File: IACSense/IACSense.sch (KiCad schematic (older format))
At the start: 86 parts, among them P1 IN, P2 OUT, P3 zcd, P4 event, P5 Prog, P6 +3.3v, P7 I2C, P8 Test, SW1 SW_Push, U1 MCP39F521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

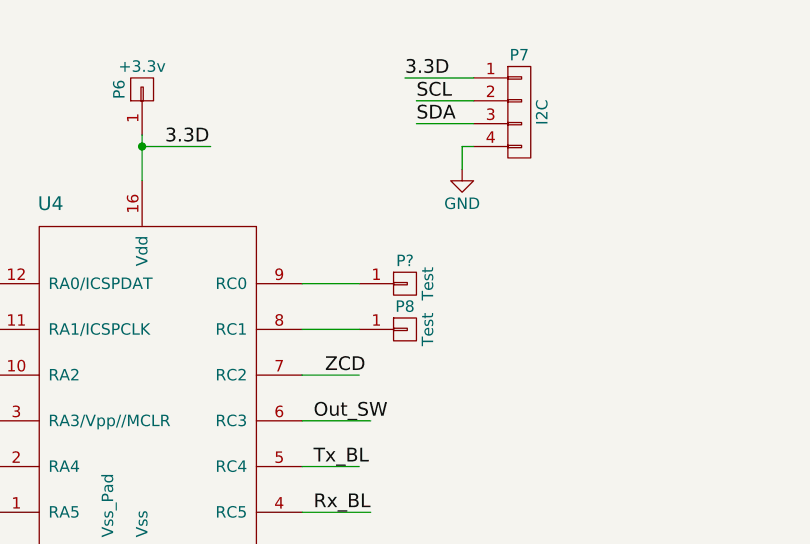
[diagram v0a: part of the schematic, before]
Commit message: place all components on DAC_Analog
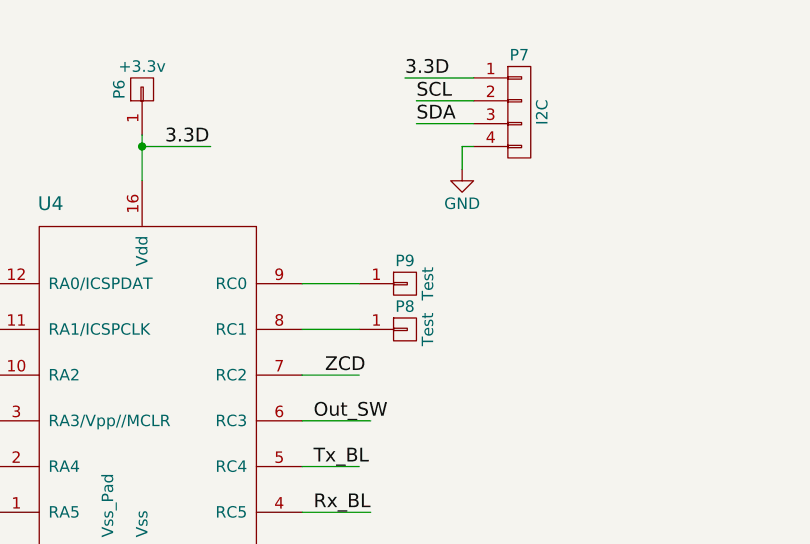
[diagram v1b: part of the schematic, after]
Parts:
- P7: footprint Pin_Headers:Pin_Header_Straight_1x04_Pitch1.00mm -> Pin_Headers:Pin_Header_Straight_1x04_Pitch1.27mm
- gave numbers to parts that had none: 1
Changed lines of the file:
@@
 $EndComp
 $Comp
-L GND #PWR2
+L GND #PWR01
 U 1 1 56D34A90
 P 3700 1950
-F 0 "#PWR2" H 3700 1700 50  0001 C CNN
+F 0 "#PWR01" H 3700 1700 50  0001 C CNN
 F 1 "GND" H 3700 1800 50  0000 C CNN
 F 2 "" H 3700 1950 60  0000 C CNN
@@
 $EndComp
 $Comp
-L GND #PWR4
+L GND #PWR02
 U 1 1 56D35186
 P 4750 2950
-F 0 "#PWR4" H 4750 2700 50  0001 C CNN
+F 0 "#PWR02" H 4750 2700 50  0001 C CNN
 F 1 "GND" H 4750 2800 50  0000 C CNN
 F 2 "" H 4750 2950 60  0000 C CNN
@@
 $EndComp
 $Comp
-L GND #PWR3
+L GND #PWR03
 U 1 1 56D35ED8
 P 4350 3900
-F 0 "#PWR3" H 4350 3650 50  0001 C CNN
+F 0 "#PWR03" H 4350 3650 50  0001 C CNN
 F 1 "GND" H 4350 3750 50  0000 C CNN
 F 2 "" H 4350 3900 60  0000 C CNN
@@
 $EndComp
 $Comp
-L GND #PWR5
+L GND #PWR04
 U 1 1 56D366F0
 P 4950 4750
-F 0 "#PWR5" H 4950 4500 50  0001 C CNN
+F 0 "#PWR04" H 4950 4500 50  0001 C CNN
 F 1 "GND" H 4950 4600 50  0000 C CNN
 F 2 "" H 4950 4750 60  0000 C CNN
@@
 $EndComp
 $Comp
-L GND #PWR8
+L GND #PWR05
 U 1 1 56D36767
 P 5250 4750
-F 0 "#PWR8" H 5250 4500 50  0001 C CNN
+F 0 "#PWR05" H 5250 4500 50  0001 C CNN
 F 1 "GND" H 5250 4600 50  0000 C CNN
 F 2 "" H 5250 4750 60  0000 C CNN
@@
 $EndComp
 $Comp
-L GND #PWR14
+L GND #PWR06
 U 1 1 56D37BE1
 P 7000 2750
-F 0 "#PWR14" H 7000 2500 50  0001 C CNN
+F 0 "#PWR06" H 7000 2500 50  0001 C CNN
 F 1 "GND" H 7000 2600 50  0000 C CNN
 F 2 "" H 7000 2750 60  0000 C CNN
@@
 $EndComp
 $Comp
-L GND #PWR10
+L GND #PWR07
 U 1 1 56D38721
 P 5900 4300
-F 0 "#PWR10" H 5900 4050 50  0001 C CNN
+F 0 "#PWR07" H 5900 4050 50  0001 C CNN
 F 1 "GND" H 5900 4150 50  0000 C CNN
 F 2 "" H 5900 4300 60  0000 C CNN
@@
 $EndComp
 $Comp
-L GND #PWR11
+L GND #PWR08
 U 1 1 56D3887C
 P 6000 4500
-F 0 "#PWR11" H 6000 4250 50  0001 C CNN
+F 0 "#PWR08" H 6000 4250 50  0001 C CNN
 F 1 "GND" H 6000 4350 50  0000 C CNN
 F 2 "" H 6000 4500 60  0000 C CNN
@@
 $EndComp
 $Comp
-L GND #PWR12
+L GND #PWR09
 U 1 1 56D38905
 P 6200 4300
-F 0 "#PWR12" H 6200 4050 50  0001 C CNN
+F 0 "#PWR09" H 6200 4050 50  0001 C CNN
 F 1 "GND" H 6200 4150 50  0000 C CNN
 F 2 "" H 6200 4300 60  0000 C CNN
@@
 $EndComp
 $Comp
-L GND #PWR13
+L GND #PWR010
 U 1 1 56D38BD8
 P 6850 4250
-F 0 "#PWR13" H 6850 4000 50  0001 C CNN
+F 0 "#PWR010" H 6850 4000 50  0001 C CNN
 F 1 "GND" H 6850 4100 50  0000 C CNN
 F 2 "" H 6850 4250 60  0000 C CNN
@@
 $EndComp
 $Comp
-L GND #PWR15
+L GND #PWR011
 U 1 1 56D38CDF
 P 7150 4250
-F 0 "#PWR15" H 7150 4000 50  0001 C CNN
+F 0 "#PWR011" H 7150 4000 50  0001 C CNN
 F 1 "GND" H 7150 4100 50  0000 C CNN
 F 2 "" H 7150 4250 60  0000 C CNN
@@
 $EndComp
 $Comp
-L GND #PWR17
+L GND #PWR012
 U 1 1 56D3A7BB
 P 7750 4350
-F 0 "#PWR17" H 7750 4100 50  0001 C CNN
+F 0 "#PWR012" H 7750 4100 50  0001 C CNN
 F 1 "GND" H 7750 4200 50  0000 C CNN
 F 2 "" H 7750 4350 60  0000 C CNN
@@
 $EndComp
 $Comp
-L GND #PWR20
+L GND #PWR013
 U 1 1 56D3A84D
 P 8150 4600
-F 0 "#PWR20" H 8150 4350 50  0001 C CNN
+F 0 "#PWR013" H 8150 4350 50  0001 C CNN
 F 1 "GND" H 8150 4450 50  0000 C CNN
 F 2 "" H 8150 4600 60  0000 C CNN
@@
 $EndComp
 $Comp
-L GND #PWR22
+L GND #PWR014
 U 1 1 56D3A8DF
 P 9000 4600
-F 0 "#PWR22" H 9000 4350 50  0001 C CNN
+F 0 "#PWR014" H 9000 4350 50  0001 C CNN
 F 1 "GND" H 9000 4450 50  0000 C CNN
 F 2 "" H 9000 4600 60  0000 C CNN
@@
 $EndComp
 $Comp
-L GND #PWR25
+L GND #PWR015
 U 1 1 56D3C1EB
 P 9750 5850
-F 0 "#PWR25" H 9750 5600 50  0001 C CNN
+F 0 "#PWR015" H 9750 5600 50  0001 C CNN
 F 1 "GND" H 9750 5700 50  0000 C CNN
 F 2 "" H 9750 5850 60  0000 C CNN
@@
 $EndComp
 $Comp
-L GND #PWR28
+L GND #PWR016
 U 1 1 56D3C292
 P 10400 5850
-F 0 "#PWR28" H 10400 5600 50  0001 C CNN
+F 0 "#PWR016" H 10400 5600 50  0001 C CNN
 F 1 "GND" H 10400 5700 50  0000 C CNN
 F 2 "" H 10400 5850 60  0000 C CNN
@@
 $EndComp
 $Comp
-L GND #PWR16
+L GND #PWR017
 U 1 1 56D3C339
 P 7550 1250
-F 0 "#PWR16" H 7550 1000 50  0001 C CNN
+F 0 "#PWR017" H 7550 1000 50  0001 C CNN
 F 1 "GND" H 7550 1100 50  0000 C CNN
 F 2 "" H 7550 1250 60  0000 C CNN
@@
 $EndComp
 $Comp
-L GND #PWR6
+L GND #PWR018
 U 1 1 56D3C47C
 P 5000 1100
-F 0 "#PWR6" H 5000 850 50  0001 C CNN
+F 0 "#PWR018" H 5000 850 50  0001 C CNN
 F 1 "GND" H 5000 950 50  0000 C CNN
 F 2 "" H 5000 1100 60  0000 C CNN
@@
 $EndComp
 $Comp
-L GND #PWR7
+L GND #PWR019
 U 1 1 56D3C523
 P 5250 1100
-F 0 "#PWR7" H 5250 850 50  0001 C CNN
+F 0 "#PWR019" H 5250 850 50  0001 C CNN
 F 1 "GND" H 5250 950 50  0000 C CNN
 F 2 "" H 5250 1100 60  0000 C CNN
@@
 3.3D
 $Comp
-L GND #PWR21
+L GND #PWR020
 U 1 1 56D37A29
 P 8750 1300
-F 0 "#PWR21" H 8750 1050 50  0001 C CNN
+F 0 "#PWR020" H 8750 1050 50  0001 C CNN
 F 1 "GND" H 8750 1150 50  0000 C CNN
 F 2 "" H 8750 1300 60  0000 C CNN
@@
 $EndComp
 $Comp
-L GND #PWR23
+L GND #PWR021
 U 1 1 56D3842E
 P 9300 3750
-F 0 "#PWR23" H 9300 3500 50  0001 C CNN
+F 0 "#PWR021" H 9300 3500 50  0001 C CNN
 F 1 "GND" H 9300 3600 50  0000 C CNN
 F 2 "" H 9300 3750 60  0000 C CNN
@@
 $EndComp
 $Comp
-L GND #PWR24
+L GND #PWR022
 U 1 1 56D38434
 P 9600 3750
-F 0 "#PWR24" H 9600 3500 50  0001 C CNN
+F 0 "#PWR022" H 9600 3500 50  0001 C CNN
 F 1 "GND" H 9600 3600 50  0000 C CNN
 F 2 "" H 9600 3750 60  0000 C CNN
@@
 $EndComp
 $Comp
-L GND #PWR27
+L GND #PWR023
 U 1 1 56D3877B
 P 10000 3100
-F 0 "#PWR27" H 10000 2850 50  0001 C CNN
+F 0 "#PWR023" H 10000 2850 50  0001 C CNN
 F 1 "GND" H 10000 2950 50  0000 C CNN
 F 2 "" H 10000 3100 60  0000 C CNN
@@
 $EndComp
 $Comp
-L GND #PWR36
+L GND #PWR024
 U 1 1 56D39A08
 P 14950 6400
-F 0 "#PWR36" H 14950 6150 50  0001 C CNN
+F 0 "#PWR024" H 14950 6150 50  0001 C CNN
 F 1 "GND" H 14950 6250 50  0000 C CNN
 F 2 "" H 14950 6400 60  0000 C CNN
@@
 SDA
 $Comp
-L GND #PWR29
+L GND #PWR025
 U 1 1 56DBE06C
 P 11400 1200
-F 0 "#PWR29" H 11400 950 50  0001 C CNN
+F 0 "#PWR025" H 11400 950 50  0001 C CNN
 F 1 "GND" H 11400 1050 50  0000 C CNN
 F 2 "" H 11400 1200 60  0000 C CNN
@@
 $EndComp
 $Comp
-L GND #PWR18
+L GND #PWR026
 U 1 1 57743D9C
 P 7850 1250
-F 0 "#PWR18" H 7850 1000 50  0001 C CNN
+F 0 "#PWR026" H 7850 1000 50  0001 C CNN
 F 1 "GND" H 7850 1100 50  0000 C CNN
 F 2 "" H 7850 1250 60  0000 C CNN
@@
 F 0 "P7" H 11650 1200 50  0000 C CNN
 F 1 "I2C" V 11750 950 50  0000 C CNN
-F 2 "Pin_Headers:Pin_Header_Straight_1x04_Pitch1.00mm" H 11650 950 50  0001 C CNN
+F 2 "Pin_Headers:Pin_Header_Straight_1x04_Pitch1.27mm" H 11650 950 50  0001 C CNN
 F 3 "" H 11650 950 50  0000 C CNN
 	1    11650 950
@@
 3.3D
 $Comp
-L GND #PWR26
+L GND #PWR027
 U 1 1 57843F08
 P 9850 3100
-F 0 "#PWR26" H 9850 2850 50  0001 C CNN
+F 0 "#PWR027" H 9850 2850 50  0001 C CNN
 F 1 "GND" H 9850 2950 50  0000 C CNN
 F 2 "" H 9850 3100 60  0000 C CNN
@@
 $EndComp
 $Comp
-L GND #PWR9
+L GND #PWR028
 U 1 1 57844CD3
 P 5800 4500
-F 0 "#PWR9" H 5800 4250 50  0001 C CNN
+F 0 "#PWR028" H 5800 4250 50  0001 C CNN
 F 1 "GND" H 5800 4350 50  0000 C CNN
 F 2 "" H 5800 4500 60  0000 C CNN
@@
 $EndComp
 $Comp
-L GND #PWR34
+L GND #PWR029
 U 1 1 59D640C6
 P 14000 4400
-F 0 "#PWR34" H 14000 4150 50  0001 C CNN
+F 0 "#PWR029" H 14000 4150 50  0001 C CNN
 F 1 "GND" H 14000 4250 50  0000 C CNN
 F 2 "" H 14000 4400 60  0000 C CNN
@@
 Connection ~ 12750 5250
 $Comp
-L GND #PWR30
+L GND #PWR030
 U 1 1 59D64EEA
 P 12150 5350
-F 0 "#PWR30" H 12150 5100 50  0001 C CNN
+F 0 "#PWR030" H 12150 5100 50  0001 C CNN
 F 1 "GND" H 12150 5200 50  0000 C CNN
 F 2 "" H 12150 5350 60  0000 C CNN
@@
 	14450 5950 14550 5950
 $Comp
-L GND #PWR35
+L GND #PWR031
 U 1 1 59D65E7E
 P 14000 6650
-F 0 "#PWR35" H 14000 6400 50  0001 C CNN
+F 0 "#PWR031" H 14000 6400 50  0001 C CNN
 F 1 "GND" H 14000 6500 50  0000 C CNN
 F 2 "" H 14000 6650 60  0000 C CNN
@@
 	14000 6550 14000 6650
 $Comp
-L GND #PWR33
+L GND #PWR032
 U 1 1 59D660E8
 P 13850 6650
-F 0 "#PWR33" H 13850 6400 50  0001 C CNN
+F 0 "#PWR032" H 13850 6400 50  0001 C CNN
 F 1 "GND" H 13850 6500 50  0000 C CNN
 F 2 "" H 13850 6650 60  0000 C CNN
@@
 	13850 6550 13850 6650
 $Comp
-L GND #PWR32
+L GND #PWR033
 U 1 1 59D6613A
 P 13700 6650
-F 0 "#PWR32" H 13700 6400 50  0001 C CNN
+F 0 "#PWR033" H 13700 6400 50  0001 C CNN
 F 1 "GND" H 13700 6500 50  0000 C CNN
 F 2 "" H 13700 6650 60  0000 C CNN
@@
 	13700 6550 13700 6650
 $Comp
-L GND #PWR31
+L GND #PWR034
 U 1 1 59D66141
 P 13550 6650
-F 0 "#PWR31" H 13550 6400 50  0001 C CNN
+F 0 "#PWR034" H 13550 6400 50  0001 C CNN
 F 1 "GND" H 13550 6500 50  0000 C CNN
 F 2 "" H 13550 6650 60  0000 C CNN
@@
 3.3D
 $Comp
-L GND #PWR37
+L GND #PWR035
 U 1 1 59D68AAC
 P 15400 6350
-F 0 "#PWR37" H 15400 6100 50  0001 C CNN
+F 0 "#PWR035" H 15400 6100 50  0001 C CNN
 F 1 "GND" H 15400 6200 50  0000 C CNN
 F 2 "" H 15400 6350 60  0000 C CNN
@@
 Connection ~ 2600 4250
 $Comp
-L GND #PWR1
+L GND #PWR036
 U 1 1 59D703DE
 P 1450 5600
-F 0 "#PWR1" H 1450 5350 50  0001 C CNN
+F 0 "#PWR036" H 1450 5350 50  0001 C CNN
 F 1 "GND" H 1450 5450 50  0000 C CNN
 F 2 "" H 1450 5600 60  0000 C CNN
@@
 Line
 $Comp
-L GND #PWR19
+L GND #PWR037
 U 1 1 59E1B7D6
 P 8000 8000
-F 0 "#PWR19" H 8000 7750 50  0001 C CNN
+F 0 "#PWR037" H 8000 7750 50  0001 C CNN
 F 1 "GND" H 8000 7850 50  0000 C CNN
 F 2 "" H 8000 8000 60  0000 C CNN
@@
 	9300 2500 9350 2500
 $Comp
-L CONN_01X01 P?
+L CONN_01X01 P9
 U 1 1 59E6384E
 P 11150 1700
-F 0 "P?" H 11150 1800 50  0000 C CNN
+F 0 "P9" H 11150 1800 50  0000 C CNN
 F 1 "Test" V 11250 1700 50  0000 C CNN
 F 2 "Pin_Headers:Pin_Header_Straight_1x01_Pitch1.00mm" H 11150 1700 60  0001 C CNN
